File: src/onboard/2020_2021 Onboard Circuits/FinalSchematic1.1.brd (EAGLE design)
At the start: 135.6 x 80 mm, 97 parts, among them IC1 A5975D, IC2 A5975D, IC3 A5975D

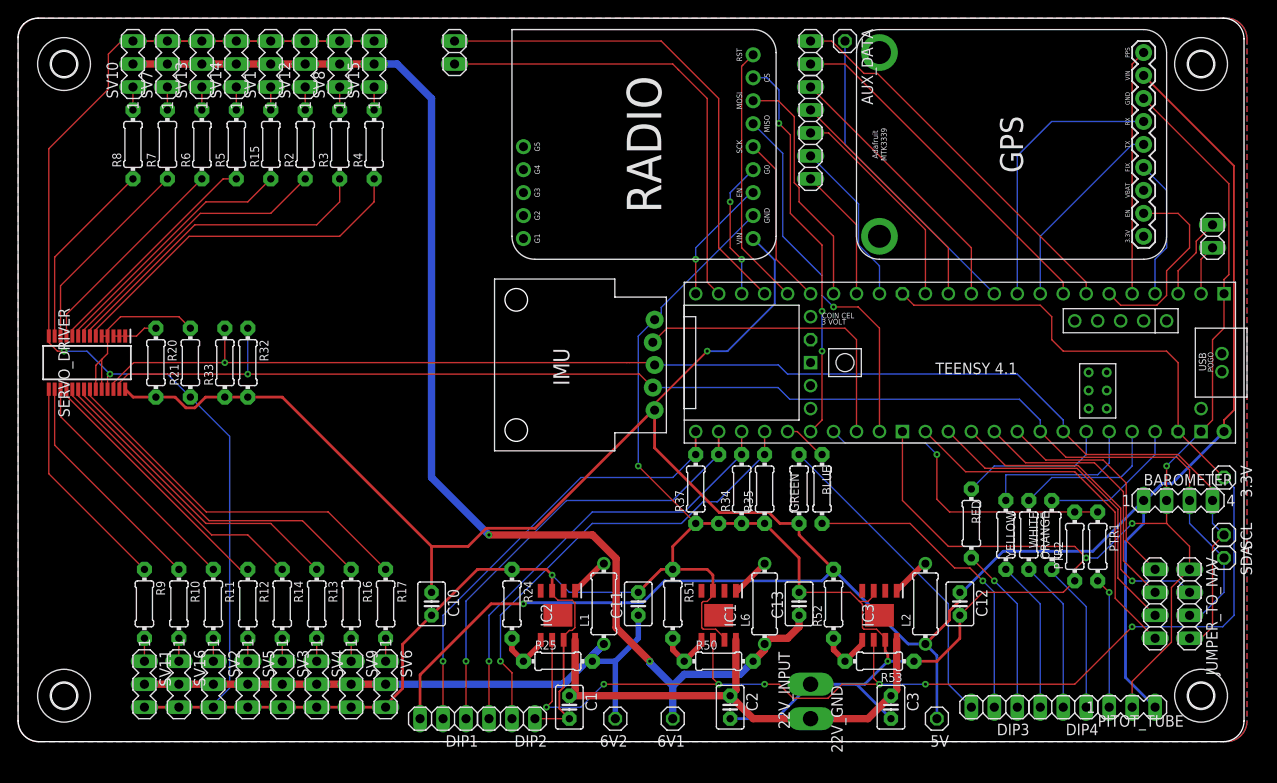
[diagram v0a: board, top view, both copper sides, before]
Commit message: Rounded corners of navigation board. Made corner radius same on both boards.
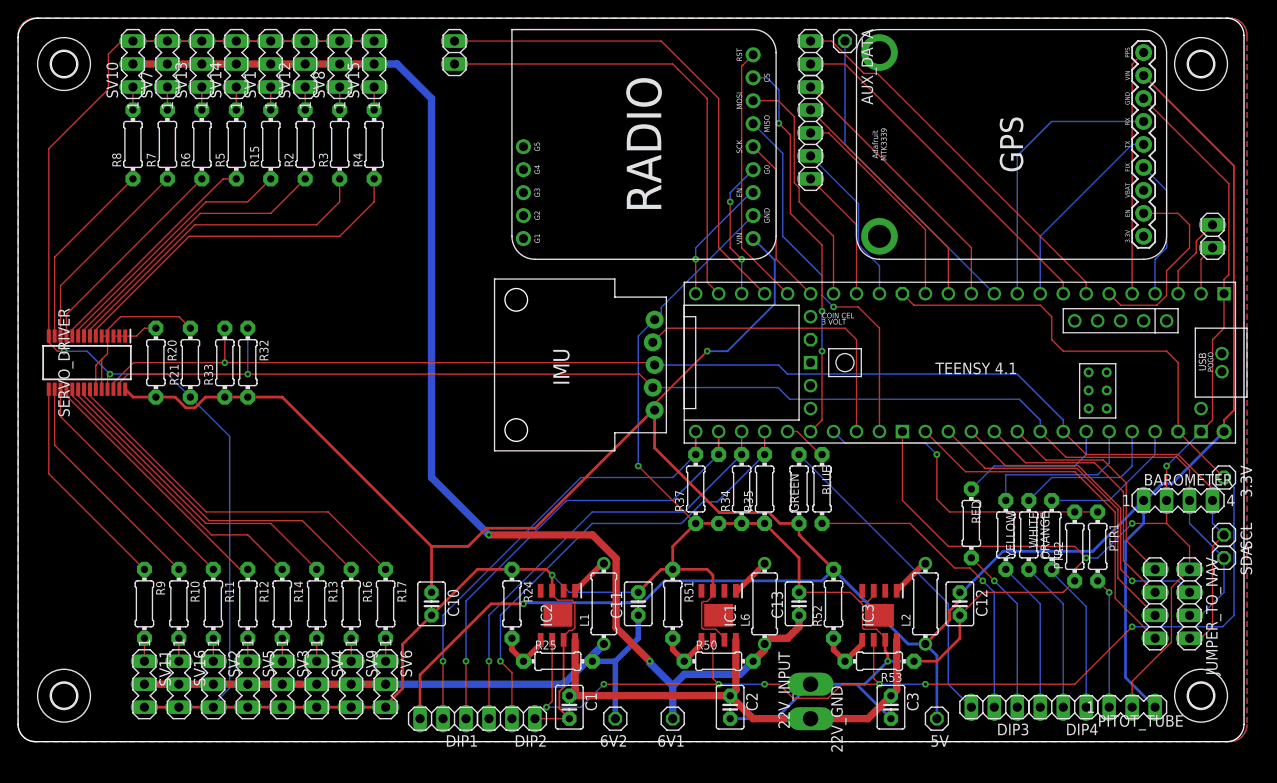
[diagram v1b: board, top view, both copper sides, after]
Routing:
- net SCL: vias 1 -> 2
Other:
- outline, holes or cut-outs redrawn
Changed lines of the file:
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@@
 <board>
 <plain>
-<wire x1="100" y1="2.286" x2="100" y2="77.714" width="0" layer="20"/>
-<wire x1="100" y1="77.714" x2="97.714" y2="80" width="0" layer="20" curve="90"/>
-<wire x1="97.714" y1="80" x2="-33.35310625" y2="80" width="0" layer="20"/>
+<wire x1="-33.655" y1="0" x2="98.095" y2="0" width="0" layer="20"/>
+<wire x1="98.095" y1="0" x2="100" y2="1.905" width="0" layer="20" curve="90"/>
+<wire x1="100" y1="1.905" x2="100" y2="78.095" width="0" layer="20"/>
+<wire x1="100" y1="78.095" x2="98.095" y2="80" width="0" layer="20" curve="90"/>
+<wire x1="98.095" y1="80" x2="-33.35310625" y2="80" width="0" layer="20"/>
 <wire x1="-33.35310625" y1="80" x2="-34.969553125" y2="79.330446875" width="0" layer="20" curve="45"/>
 <wire x1="-34.969553125" y1="79.330446875" x2="-35.56" y2="77.90498125" width="0" layer="20" curve="45"/>
-<wire x1="-35.56" y1="77.90498125" x2="-35.56" y2="2.286" width="0" layer="20"/>
-<wire x1="-35.56" y1="2.286" x2="-33.274" y2="0" width="0" layer="20" curve="90"/>
-<wire x1="-33.274" y1="0" x2="97.714" y2="0" width="0" layer="20"/>
-<wire x1="97.714" y1="0" x2="100" y2="2.286" width="0" layer="20" curve="90"/>
+<wire x1="-35.56" y1="77.90498125" x2="-35.56" y2="1.905" width="0" layer="20"/>
+<wire x1="-35.56" y1="1.905" x2="-33.655" y2="0" width="0" layer="20" curve="90"/>
 </plain>
 <attributes>
@@
 <contactref element="PITOT_TUBE" pad="3"/>
 <polygon width="0.3048" layer="16">
-<vertex x="-33.274" y="80.01"/>
-<vertex x="98.044" y="80.01" curve="-90"/>
-<vertex x="100.33" y="77.724"/>
-<vertex x="100.33" y="2.286" curve="-90"/>
-<vertex x="98.044" y="0"/>
-<vertex x="-33.274" y="0" curve="-90"/>
-<vertex x="-35.56" y="2.286"/>
-<vertex x="-35.56" y="77.724" curve="-90"/>
+<vertex x="-33.655" y="80.01"/>
+<vertex x="98.425" y="80.01" curve="-90"/>
+<vertex x="100.33" y="78.105"/>
+<vertex x="100.33" y="1.905" curve="-90"/>
+<vertex x="98.425" y="0"/>
+<vertex x="-33.655" y="0" curve="-90"/>
+<vertex x="-35.56" y="1.905"/>
+<vertex x="-35.56" y="78.105" curve="-90"/>
 </polygon>
 <via x="40.64" y="43.18" extent="1-16" drill="0.35"/>
@@
 <wire x1="-12.7" y1="45.72" x2="-12.7" y2="41.91" width="0.1524" layer="1"/>
 <via x="-12.7" y="41.91" extent="1-16" drill="0.35"/>
-<wire x1="-12.7" y1="41.91" x2="31.75" y2="41.91" width="0.1524" layer="1"/>
-<wire x1="31.75" y1="41.91" x2="32.033" y2="41.91" width="0.1524" layer="1"/>
-<wire x1="32.033" y1="41.91" x2="34.573" y2="41.91" width="0.1524" layer="1"/>
-<wire x1="34.573" y1="41.91" x2="34.827" y2="41.656" width="0.1524" layer="1"/>
+<via x="34.573" y="41.91" extent="1-16" drill="0.35"/>
+<wire x1="34.827" y1="41.656" x2="34.573" y2="41.91" width="0.1524" layer="1"/>
+<wire x1="-12.7" y1="41.91" x2="34.573" y2="41.91" width="0.1524" layer="1"/>
 </signal>
 <signal name="MOSI1">
@@
 <wire x1="95.25" y1="34.29" x2="91.44" y2="30.48" width="0.1524" layer="16"/>
 <polygon width="0.3048" layer="1">
-<vertex x="-33.274" y="80.01"/>
-<vertex x="98.044" y="80.01" curve="-90"/>
-<vertex x="100.33" y="77.724"/>
-<vertex x="100.33" y="2.286" curve="-90"/>
-<vertex x="98.044" y="0"/>
-<vertex x="-33.274" y="0" curve="-90"/>
-<vertex x="-35.56" y="2.286"/>
-<vertex x="-35.56" y="77.724" curve="-90"/>
+<vertex x="-33.655" y="80.01"/>
+<vertex x="98.425" y="80.01" curve="-90"/>
+<vertex x="100.33" y="78.105"/>
+<vertex x="100.33" y="1.905" curve="-90"/>
+<vertex x="98.425" y="0"/>
+<vertex x="-33.655" y="0" curve="-90"/>
+<vertex x="-35.56" y="1.905"/>
+<vertex x="-35.56" y="78.105" curve="-90"/>
 </polygon>
 <wire x1="45.72" y1="58.17" x2="35.56" y2="48.01" width="0.1524" layer="16"/>
@@
 <mfgpreviewcolor name="substratecolor" color="0xFF786E46"/>
 </mfgpreviewcolors>
+<errors>
+</errors>
 </board>
 </drawing>
